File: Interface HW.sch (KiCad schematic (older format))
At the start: 2 parts

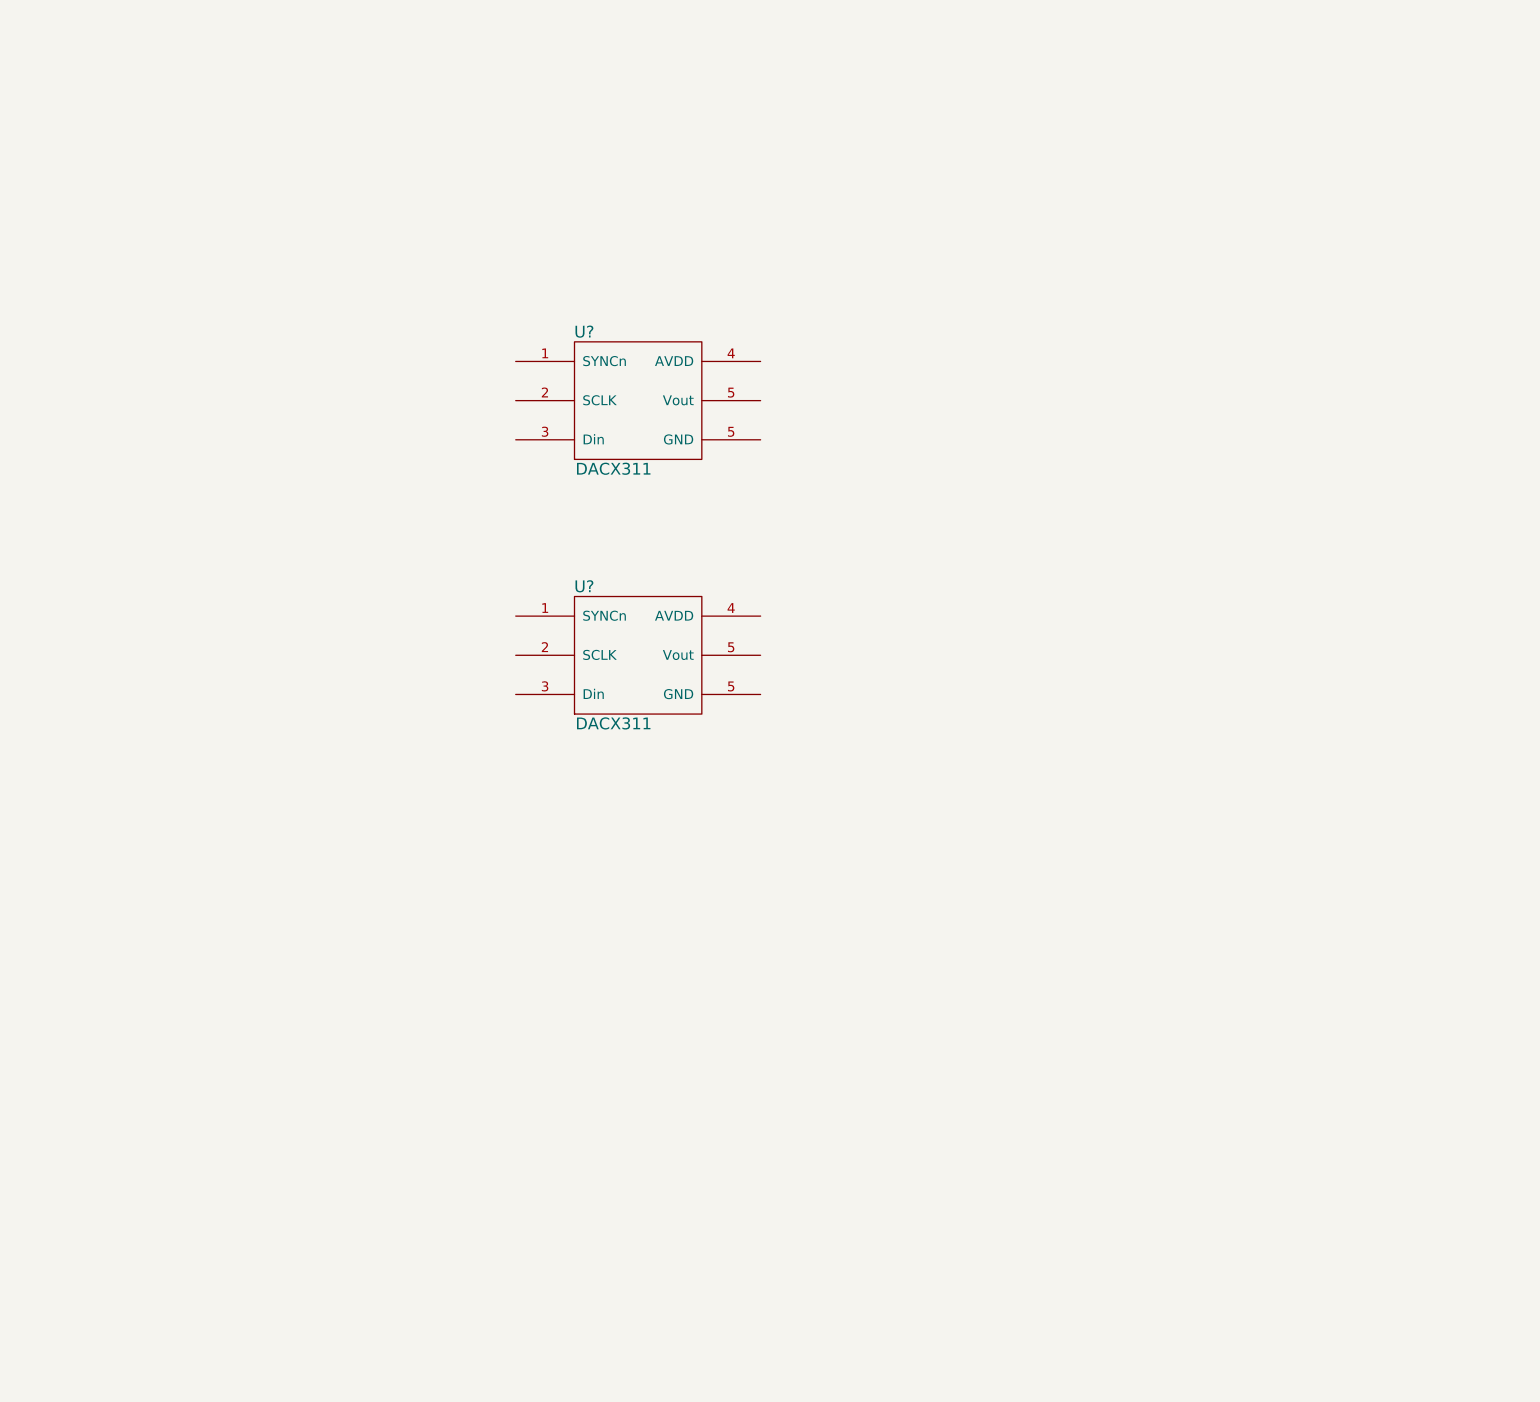
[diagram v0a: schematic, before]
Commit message: Completed pinout of controlStick
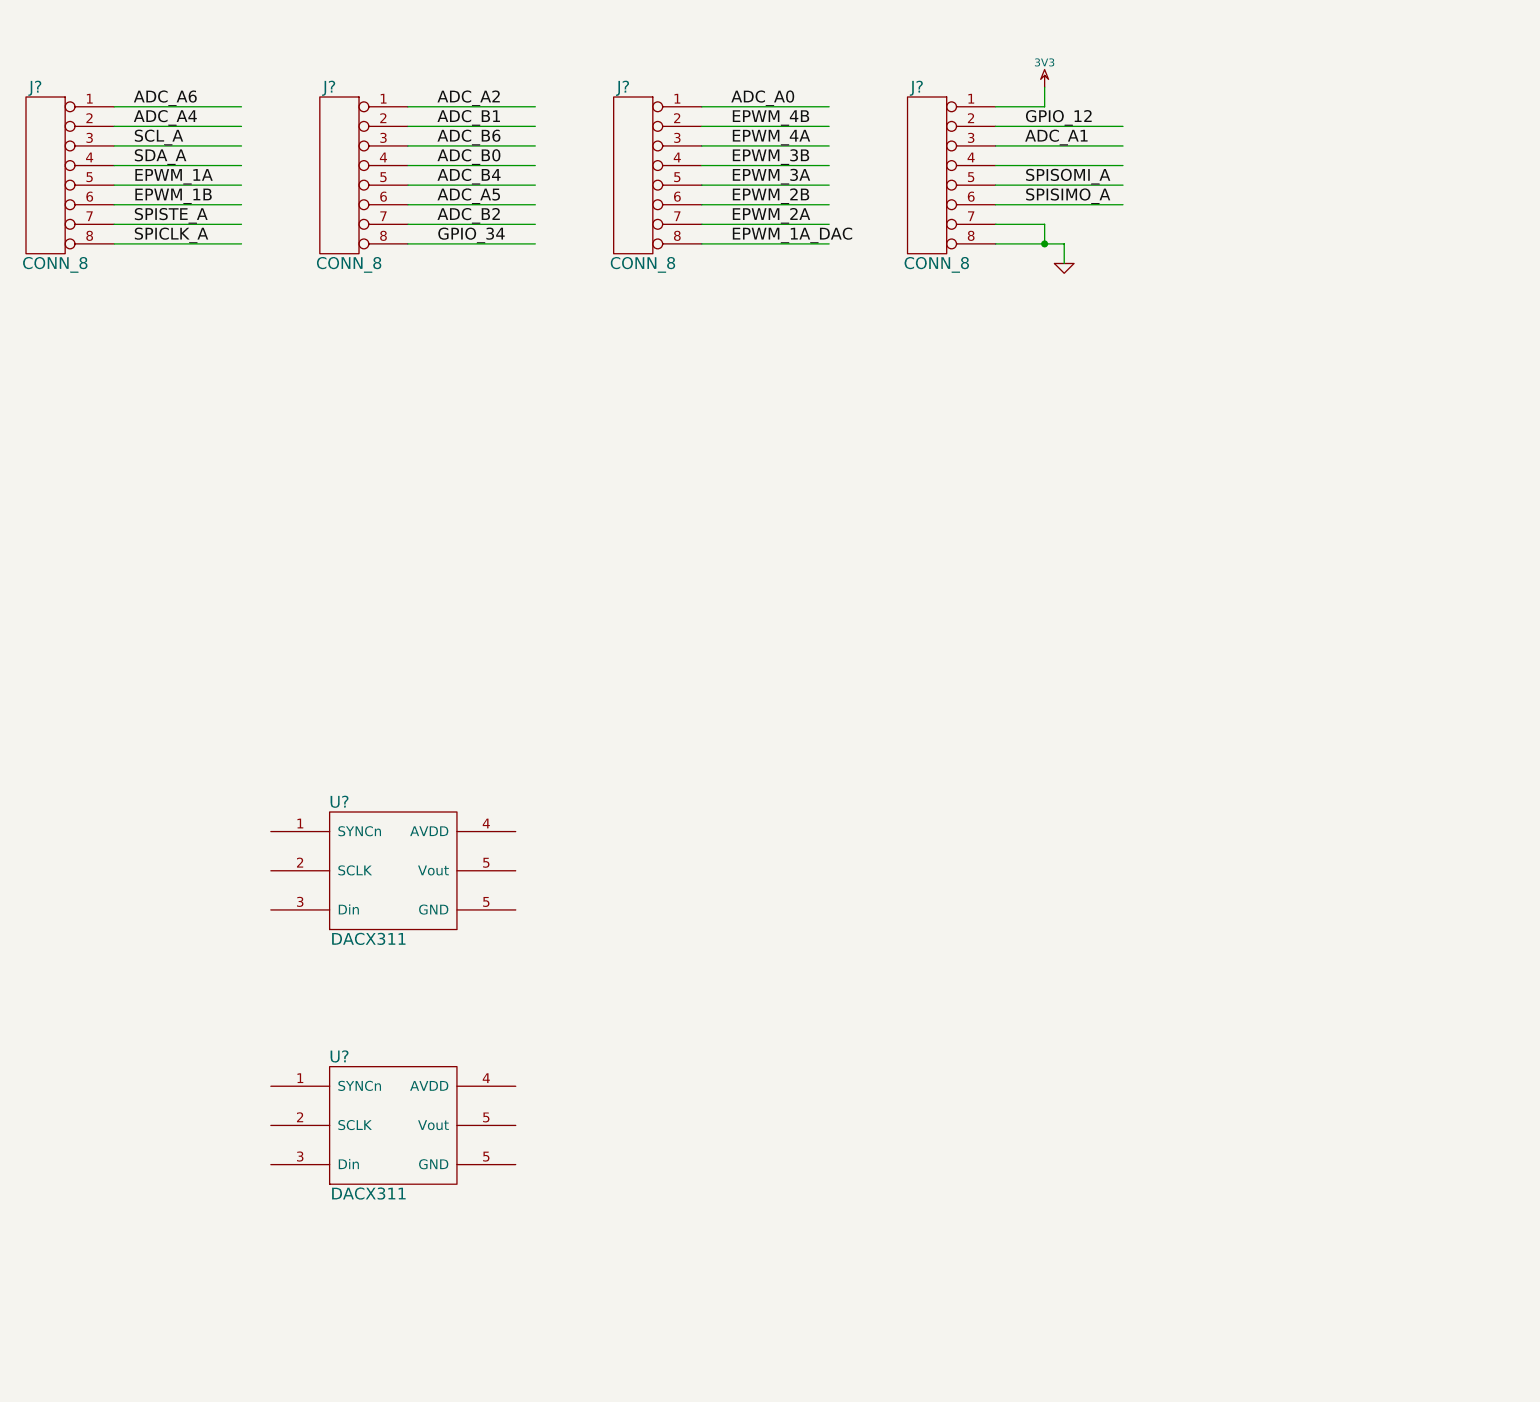
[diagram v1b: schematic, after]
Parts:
- added J? (x4): CONN_8, ~, symbol CONN_8
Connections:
- net labels added: 3V3, ADC_A0, ADC_A1, ADC_A2, ADC_A4, ADC_A5, ADC_A6, ADC_B0, ADC_B1, ADC_B2, ADC_B4, ADC_B6, EPWM_1A, EPWM_1A_DAC, EPWM_1B, EPWM_2A, EPWM_2B, EPWM_3A, EPWM_3B, EPWM_4A, EPWM_4B, GND, GPIO_12, GPIO_34, SCL_A, SDA_A, SPICLK_A, SPISIMO_A, SPISOMI_A, SPISTE_A
- wire segments 0 -> 35
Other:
- moved on the sheet: U?
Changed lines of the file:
@@
 L DACX311 U?
 U 1 1 531E5DEB
-P 3750 2450
-F 0 "U?" H 3500 2800 60  0000 C CNN
-F 1 "DACX311" H 3650 2100 60  0000 C CNN
-F 2 "" H 3750 2450 60  0000 C CNN
-F 3 "" H 3750 2450 60  0000 C CNN
-	1    3750 2450
+P 2500 4850
+F 0 "U?" H 2250 5200 60  0000 C CNN
+F 1 "DACX311" H 2400 4500 60  0000 C CNN
+F 2 "" H 2500 4850 60  0000 C CNN
+F 3 "" H 2500 4850 60  0000 C CNN
+	1    2500 4850
 	1    0    0    -1
 $EndComp
@@
 L DACX311 U?
 U 1 1 531E5DFA
-P 3750 3750
-F 0 "U?" H 3500 4100 60  0000 C CNN
-F 1 "DACX311" H 3650 3400 60  0000 C CNN
-F 2 "" H 3750 3750 60  0000 C CNN
-F 3 "" H 3750 3750 60  0000 C CNN
-	1    3750 3750
-	1    0    0    -1
-$EndComp
+P 2500 6150
+F 0 "U?" H 2250 6500 60  0000 C CNN
+F 1 "DACX311" H 2400 5800 60  0000 C CNN
+F 2 "" H 2500 6150 60  0000 C CNN
+F 3 "" H 2500 6150 60  0000 C CNN
+	1    2500 6150
+	1    0    0    -1
+$EndComp
+$Comp
+L CONN_8 J?
+U 1 1 531E6461
+P 750 1300
+F 0 "J?" H 800 1750 60  0000 C CNN
+F 1 "CONN_8" H 700 850 60  0000 C CNN
+F 2 "~" H 750 1300 60  0000 C CNN
+F 3 "~" H 750 1300 60  0000 C CNN
+	1    750  1300
+	-1   0    0    -1
+$EndComp
+$Comp
+L CONN_8 J?
+U 1 1 531E6470
+P 2250 1300
+F 0 "J?" H 2300 1750 60  0000 C CNN
+F 1 "CONN_8" H 2200 850 60  0000 C CNN
+F 2 "~" H 2250 1300 60  0000 C CNN
+F 3 "~" H 2250 1300 60  0000 C CNN
+	1    2250 1300
+	-1   0    0    -1
+$EndComp
+$Comp
+L CONN_8 J?
+U 1 1 531E647F
+P 3750 1300
+F 0 "J?" H 3800 1750 60  0000 C CNN
+F 1 "CONN_8" H 3700 850 60  0000 C CNN
+F 2 "~" H 3750 1300 60  0000 C CNN
+F 3 "~" H 3750 1300 60  0000 C CNN
+	1    3750 1300
+	-1   0    0    -1
+$EndComp
+$Comp
+L CONN_8 J?
+U 1 1 531E649D
+P 5250 1300
+F 0 "J?" H 5300 1750 60  0000 C CNN
+F 1 "CONN_8" H 5200 850 60  0000 C CNN
+F 2 "~" H 5250 1300 60  0000 C CNN
+F 3 "~" H 5250 1300 60  0000 C CNN
+	1    5250 1300
+	-1   0    0    -1
+$EndComp
+Wire Wire Line
+	2600 950  3250 950
+Wire Wire Line
+	2600 1050 3250 1050
+Wire Wire Line
+	2600 1150 3250 1150
+Wire Wire Line
+	2600 1250 3250 1250
+Wire Wire Line
+	2600 1350 3250 1350
+Wire Wire Line
+	2600 1450 3250 1450
+Wire Wire Line
+	2600 1550 3250 1550
+Wire Wire Line
+	2600 1650 3250 1650
+Wire Wire Line
+	1100 950  1750 950
+Wire Wire Line
+	1100 1050 1750 1050
+Wire Wire Line
+	1100 1150 1750 1150
+Wire Wire Line
+	1100 1250 1750 1250
+Wire Wire Line
+	1100 1350 1750 1350
+Wire Wire Line
+	1100 1450 1750 1450
+Wire Wire Line
+	1100 1550 1750 1550
+Wire Wire Line
+	1100 1650 1750 1650
+Wire Wire Line
+	4100 950  4750 950
+Wire Wire Line
+	4100 1050 4750 1050
+Wire Wire Line
+	4100 1150 4750 1150
+Wire Wire Line
+	4100 1250 4750 1250
+Wire Wire Line
+	4100 1350 4750 1350
+Wire Wire Line
+	4100 1450 4750 1450
+Wire Wire Line
+	4100 1550 4750 1550
+Wire Wire Line
+	4100 1650 4750 1650
+Wire Wire Line
+	5600 950  5850 950
+Wire Wire Line
+	5600 1050 6250 1050
+Wire Wire Line
+	5600 1150 6250 1150
+Wire Wire Line
+	5600 1250 6250 1250
+Wire Wire Line
+	5600 1350 6250 1350
+Wire Wire Line
+	5600 1450 6250 1450
+Wire Wire Line
+	5600 1550 5850 1550
+Wire Wire Line
+	5600 1650 5950 1650
+Text Label 1200 950  0    60   ~ 0
+ADC_A6
+Text Label 1200 1050 0    60   ~ 0
+ADC_A4
+Text Label 1200 1150 0    60   ~ 0
+SCL_A
+Text Label 1200 1250 0    60   ~ 0
+SDA_A
+Text Label 1200 1350 0    60   ~ 0
+EPWM_1A
+Text Label 1200 1450 0    60   ~ 0
+EPWM_1B
+Text Label 1200 1550 0    60   ~ 0
+SPISTE_A
+Text Label 1200 1650 0    60   ~ 0
+SPICLK_A
+Text Label 2750 950  0    60   ~ 0
+ADC_A2
+Text Label 2750 1050 0    60   ~ 0
+ADC_B1
+Text Label 2750 1150 0    60   ~ 0
+ADC_B6
+Text Label 2750 1250 0    60   ~ 0
+ADC_B0
+Text Label 2750 1350 0    60   ~ 0
+ADC_B4
+Text Label 2750 1450 0    60   ~ 0
+ADC_A5
+Text Label 2750 1550 0    60   ~ 0
+ADC_B2
+Text Label 2750 1650 0    60   ~ 0
+GPIO_34
+Text Label 4250 950  0    60   ~ 0
+ADC_A0
+Text Label 4250 1050 0    60   ~ 0
+EPWM_4B
+Text Label 4250 1150 0    60   ~ 0
+EPWM_4A
+Text Label 4250 1250 0    60   ~ 0
+EPWM_3B
+Text Label 4250 1350 0    60   ~ 0
+EPWM_3A
+Text Label 4250 1450 0    60   ~ 0
+EPWM_2B
+Text Label 4250 1550 0    60   ~ 0
+EPWM_2A
+Text Label 4250 1650 0    60   ~ 0
+EPWM_1A_DAC
+Text Label 5750 1050 0    60   ~ 0
+GPIO_12
+Text Label 5750 1150 0    60   ~ 0
+ADC_A1
+Text Label 5750 1350 0    60   ~ 0
+SPISOMI_A
+Text Label 5750 1450 0    60   ~ 0
+SPISIMO_A
+$Comp
+L 3V3 #PWR?
+U 1 1 531E75DC
+P 5850 850
+F 0 "#PWR?" H 5850 950 40  0001 C CNN
+F 1 "3V3" H 5850 975 40  0000 C CNN
+F 2 "" H 5850 850 60  0000 C CNN
+F 3 "" H 5850 850 60  0000 C CNN
+	1    5850 850
+	1    0    0    -1
+$EndComp
+Wire Wire Line
+	5850 950  5850 850
+$Comp
+L GND #PWR?
+U 1 1 531E760C
+P 5950 1750
+F 0 "#PWR?" H 5950 1750 30  0001 C CNN
+F 1 "GND" H 5950 1680 30  0001 C CNN
+F 2 "" H 5950 1750 60  0000 C CNN
+F 3 "" H 5950 1750 60  0000 C CNN
+	1    5950 1750
+	1    0    0    -1
+$EndComp
+Wire Wire Line
+	5850 1650 5850 1550
+Wire Wire Line
+	5950 1650 5950 1750
+Connection ~ 5850 1650
 $EndSCHEMATC

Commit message: Added op-amp, and op-amp datasheet
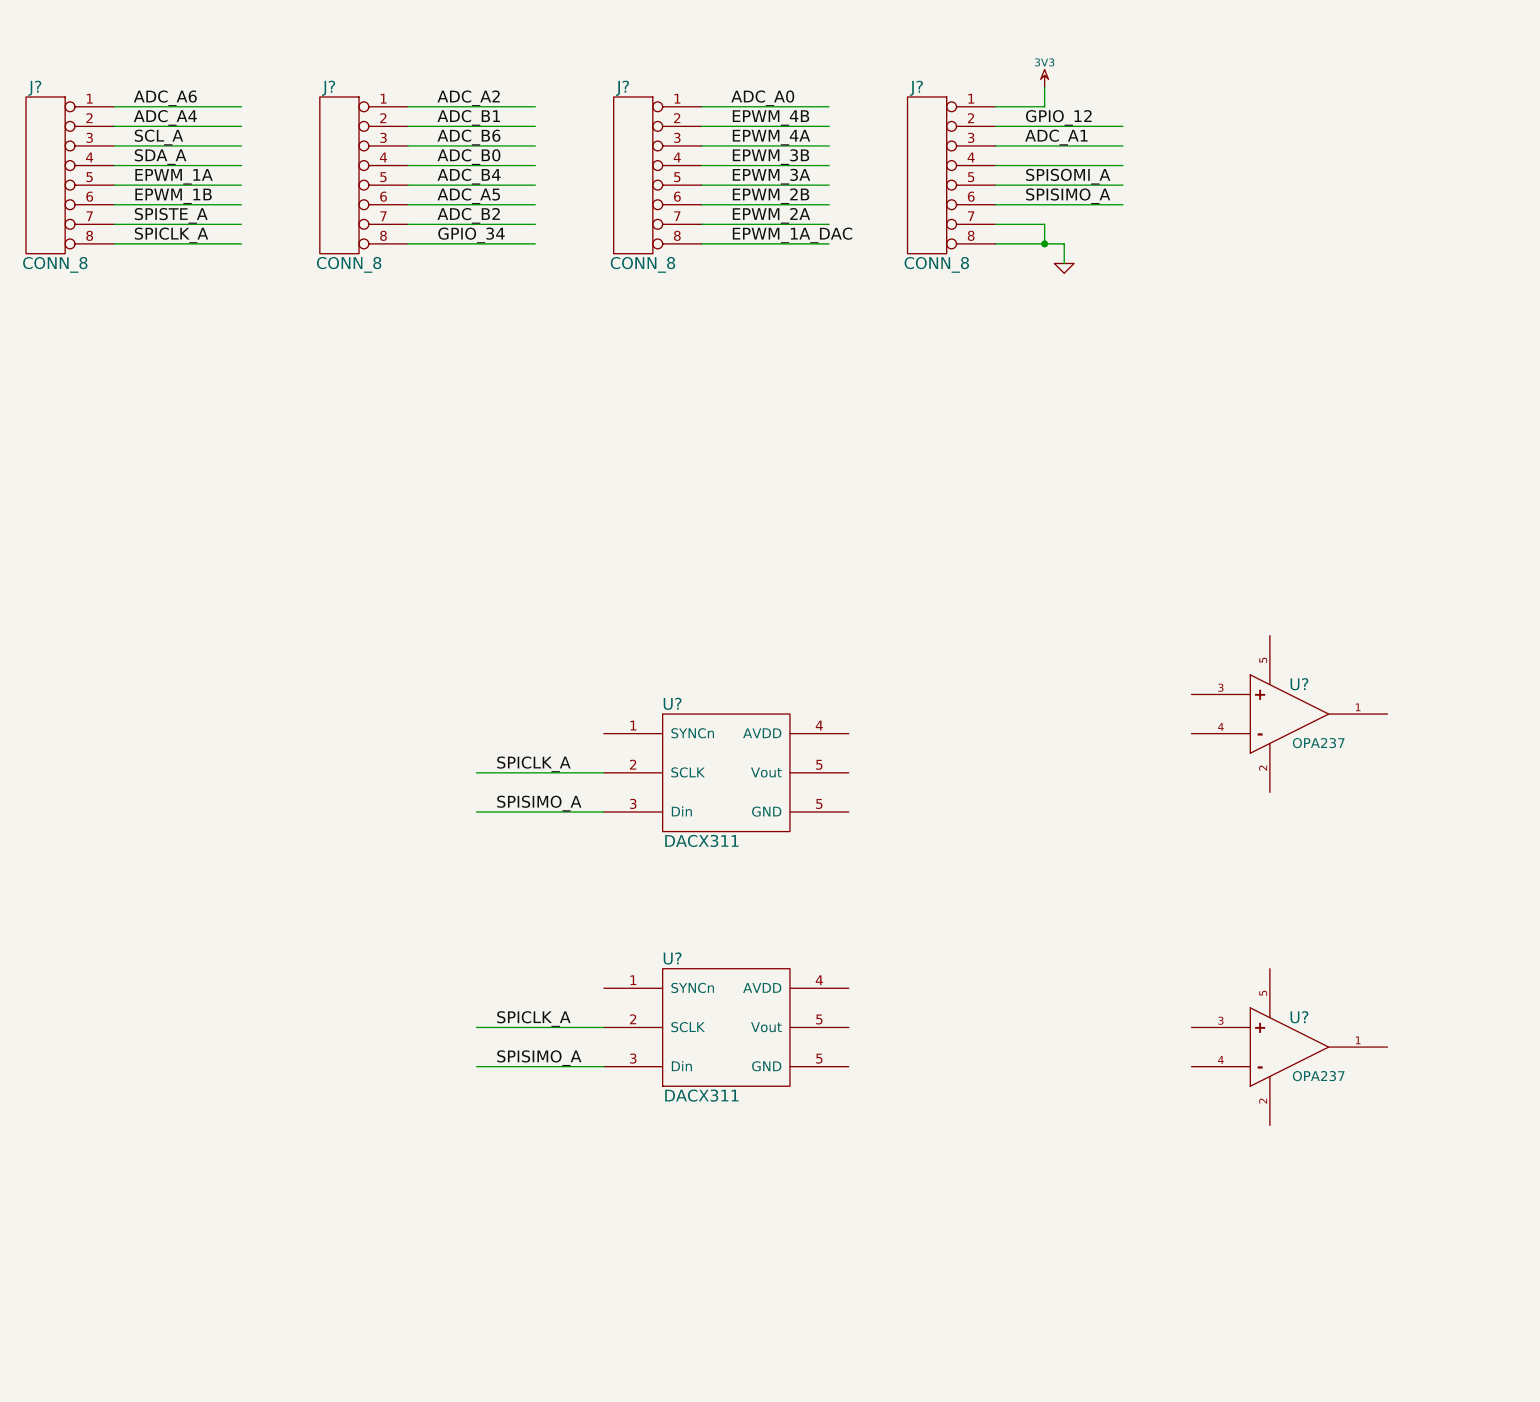
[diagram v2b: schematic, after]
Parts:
- added U? (x2): OPA237, symbol OPA237
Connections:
- wire segments 35 -> 40
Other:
- moved on the sheet: U?
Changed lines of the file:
@@
 L DACX311 U?
 U 1 1 531E5DEB
-P 2500 4850
-F 0 "U?" H 2250 5200 60  0000 C CNN
-F 1 "DACX311" H 2400 4500 60  0000 C CNN
-F 2 "" H 2500 4850 60  0000 C CNN
-F 3 "" H 2500 4850 60  0000 C CNN
-	1    2500 4850
+P 4200 4350
+F 0 "U?" H 3950 4700 60  0000 C CNN
+F 1 "DACX311" H 4100 4000 60  0000 C CNN
+F 2 "" H 4200 4350 60  0000 C CNN
+F 3 "" H 4200 4350 60  0000 C CNN
+	1    4200 4350
 	1    0    0    -1
 $EndComp
@@
 L DACX311 U?
 U 1 1 531E5DFA
-P 2500 6150
-F 0 "U?" H 2250 6500 60  0000 C CNN
-F 1 "DACX311" H 2400 5800 60  0000 C CNN
-F 2 "" H 2500 6150 60  0000 C CNN
-F 3 "" H 2500 6150 60  0000 C CNN
-	1    2500 6150
+P 4200 5650
+F 0 "U?" H 3950 6000 60  0000 C CNN
+F 1 "DACX311" H 4100 5300 60  0000 C CNN
+F 2 "" H 4200 5650 60  0000 C CNN
+F 3 "" H 4200 5650 60  0000 C CNN
+	1    4200 5650
 	1    0    0    -1
 $EndComp
@@
 	5600 1550 5850 1550
 Wire Wire Line
-	5600 1650 5950 1650
+	5600 1650 5850 1650
+Wire Wire Line
+	5850 1650 5950 1650
 Text Label 1200 950  0    60   ~ 0
 ADC_A6
@@
 	5950 1650 5950 1750
 Connection ~ 5850 1650
+Wire Wire Line
+	2950 4350 3600 4350
+Text Label 3050 4350 0    60   ~ 0
+SPICLK_A
+Wire Wire Line
+	2950 5650 3600 5650
+Text Label 3050 5650 0    60   ~ 0
+SPICLK_A
+Wire Wire Line
+	2950 4550 3600 4550
+Text Label 3050 4550 0    60   ~ 0
+SPISIMO_A
+Wire Wire Line
+	2950 5850 3600 5850
+Text Label 3050 5850 0    60   ~ 0
+SPISIMO_A
+$Comp
+L OPA237 U?
+U 1 1 531E8718
+P 7100 4050
+F 0 "U?" H 7150 4200 60  0000 C CNN
+F 1 "OPA237" H 7250 3900 50  0000 C CNN
+F 2 "" H 7100 4050 60  0000 C CNN
+F 3 "" H 7100 4050 60  0000 C CNN
+	1    7100 4050
+	1    0    0    -1
+$EndComp
+$Comp
+L OPA237 U?
+U 1 1 531E8727
+P 7100 5750
+F 0 "U?" H 7150 5900 60  0000 C CNN
+F 1 "OPA237" H 7250 5600 50  0000 C CNN
+F 2 "" H 7100 5750 60  0000 C CNN
+F 3 "" H 7100 5750 60  0000 C CNN
+	1    7100 5750
+	1    0    0    -1
+$EndComp
 $EndSCHEMATC
